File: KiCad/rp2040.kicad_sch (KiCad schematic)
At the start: 32 parts, among them SW1 SW_Push, U1 RP2040, U2 W25Q16JVUXIQ, Y1 12.000MHz-ABM8-272-T3

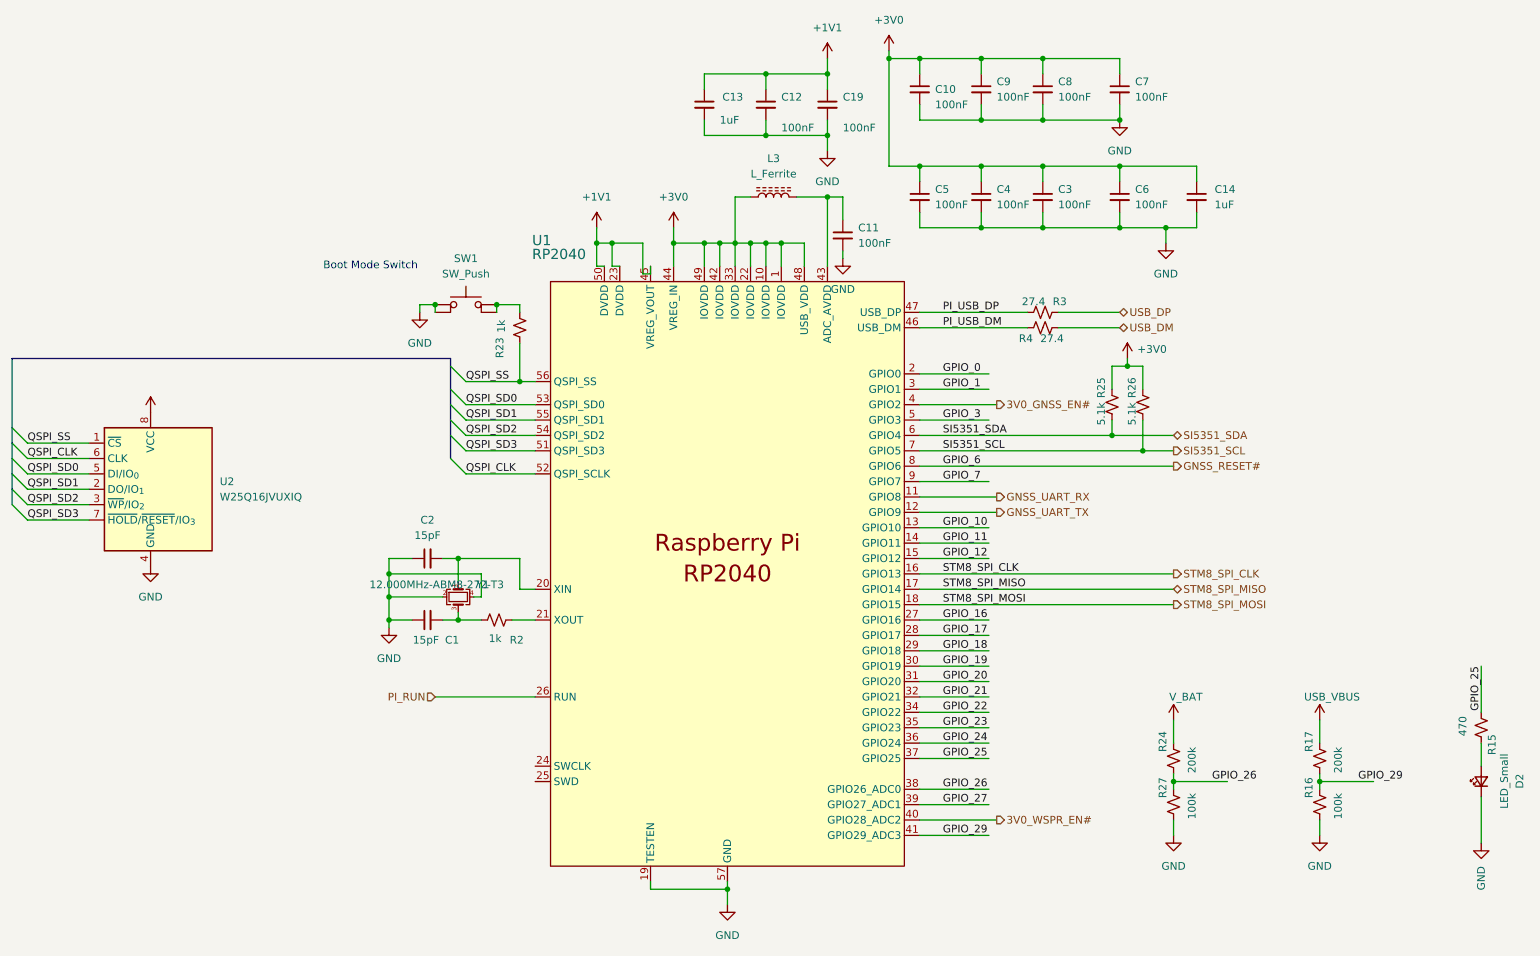
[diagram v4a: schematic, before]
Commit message: Clean up ERC errors
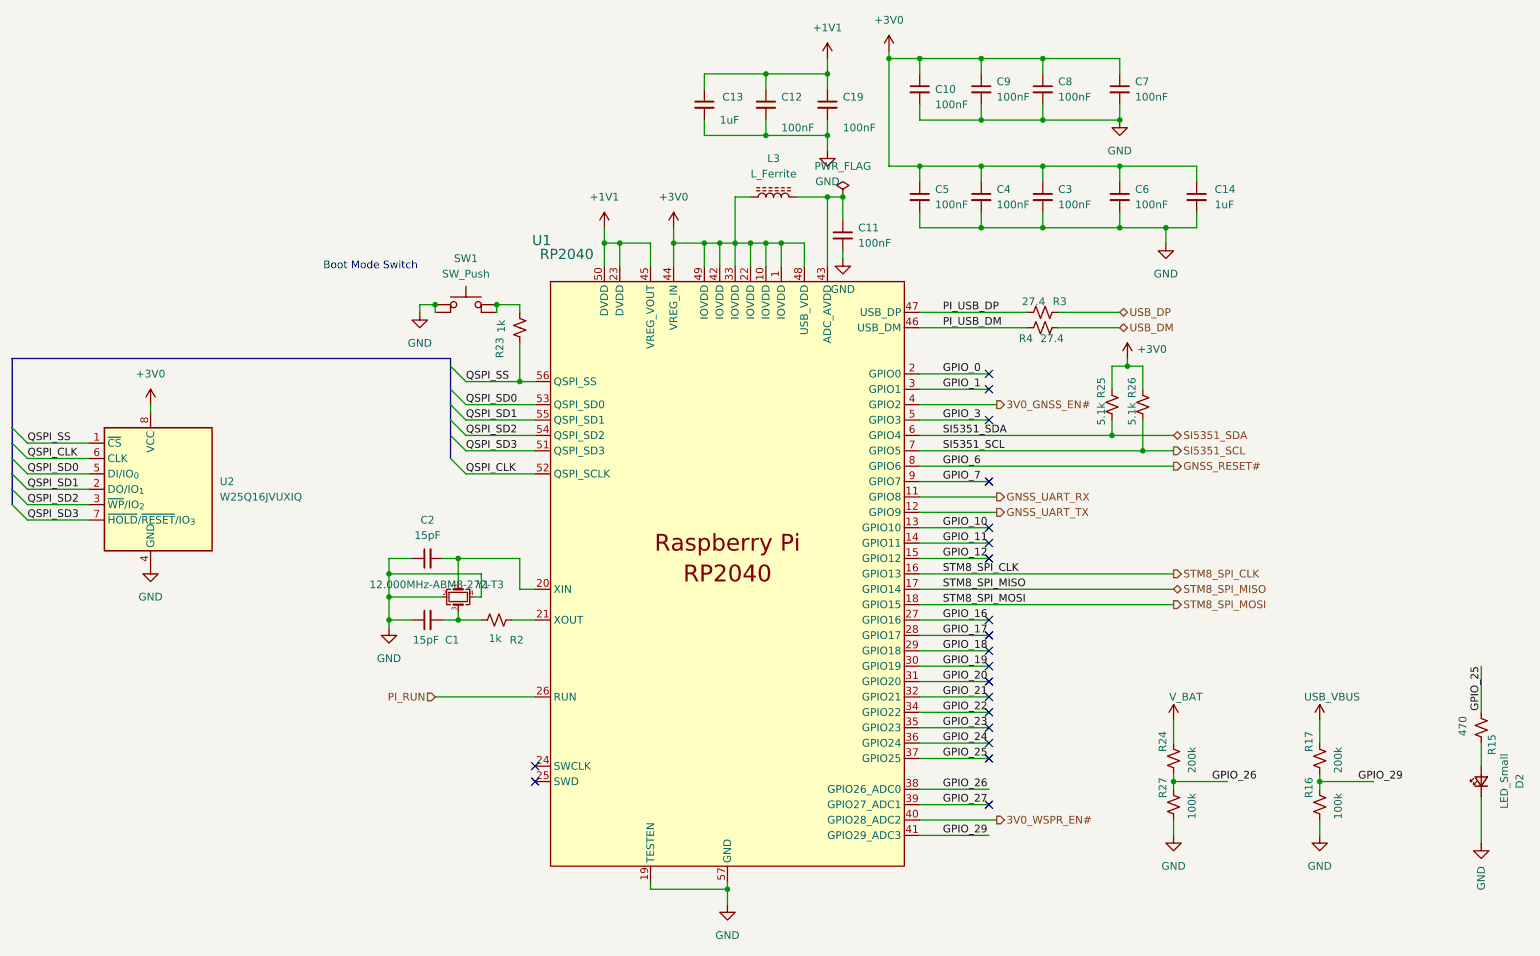
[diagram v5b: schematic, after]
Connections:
- net +3V3 is gone; now on net +3V0: U2.8 (VCC)
- no-connect marks 0 -> 20

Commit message: DRC cleanup
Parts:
- removed R25, R26: 5.1k, Resistor_SMD:R_0402_1005Metric, symbol Device:R_Small_US
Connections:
- net QSPI_CLK renamed QSPI.CLK
- net QSPI_SD0 renamed QSPI.SD0
- net QSPI_SD1 renamed QSPI.SD1
- net QSPI_SD2 renamed QSPI.SD2
- net QSPI_SD3 renamed QSPI.SD3
- net QSPI_SS renamed QSPI.SS
- no-connect marks 20 -> 19
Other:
- moved on the sheet: C12, C13, C19, R16, R17, R24, R27

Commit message: Mods
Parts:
- SW1: symbol Switch:SW_Push -> JetBoard:SW_Push
- U1: symbol RP2040 -> JetBoard:RP2040
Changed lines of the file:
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@@
 		)
 	)
-	(label "QSPI{SS, CLK, SD0, SD1, SD2, SD3}"
+	(label "QSPI{SS, CLK, SD[0..3]}"
 		(at 64.77 72.39 0)
 		(effects
@@
 	)
 	(symbol
-		(lib_id "RP2040")
+		(lib_id "JetBoard:RP2040")
 		(at 151.13 110.49 0)
 		(unit 1)
@@
 	)
 	(symbol
-		(lib_id "Switch:SW_Push")
+		(lib_id "JetBoard:SW_Push")
 		(at 107.95 63.5 0)
 		(unit 1)
